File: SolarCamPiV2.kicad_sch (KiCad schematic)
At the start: 95 parts, among them J1 TagConnect_TC2030_SWD, J2 RPi, J3 FTDI_RPI, Q1 AO3401A, Q2 AO3401A, Q3 2N7002, Q4 AO3401A, Q5 2N7002, Q6 BSS84, SW1 User, U1 CN3767, U2 HT7533, U3 SY8113B, U4 STM32G031Fx, Y1 32.768kHz

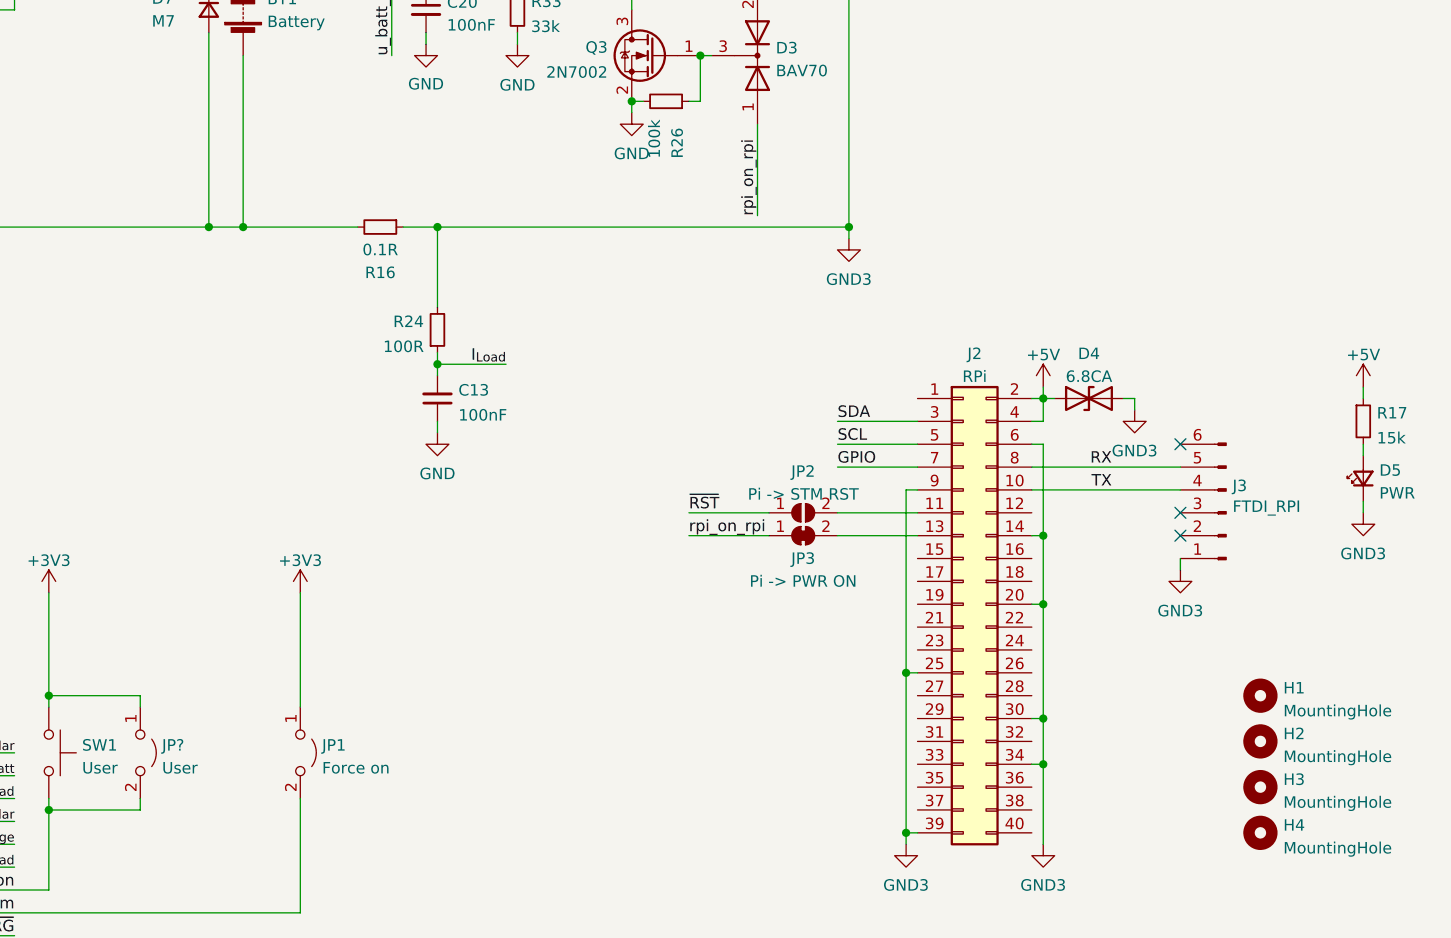
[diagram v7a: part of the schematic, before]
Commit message: Connect SWD to RPi GPIOs
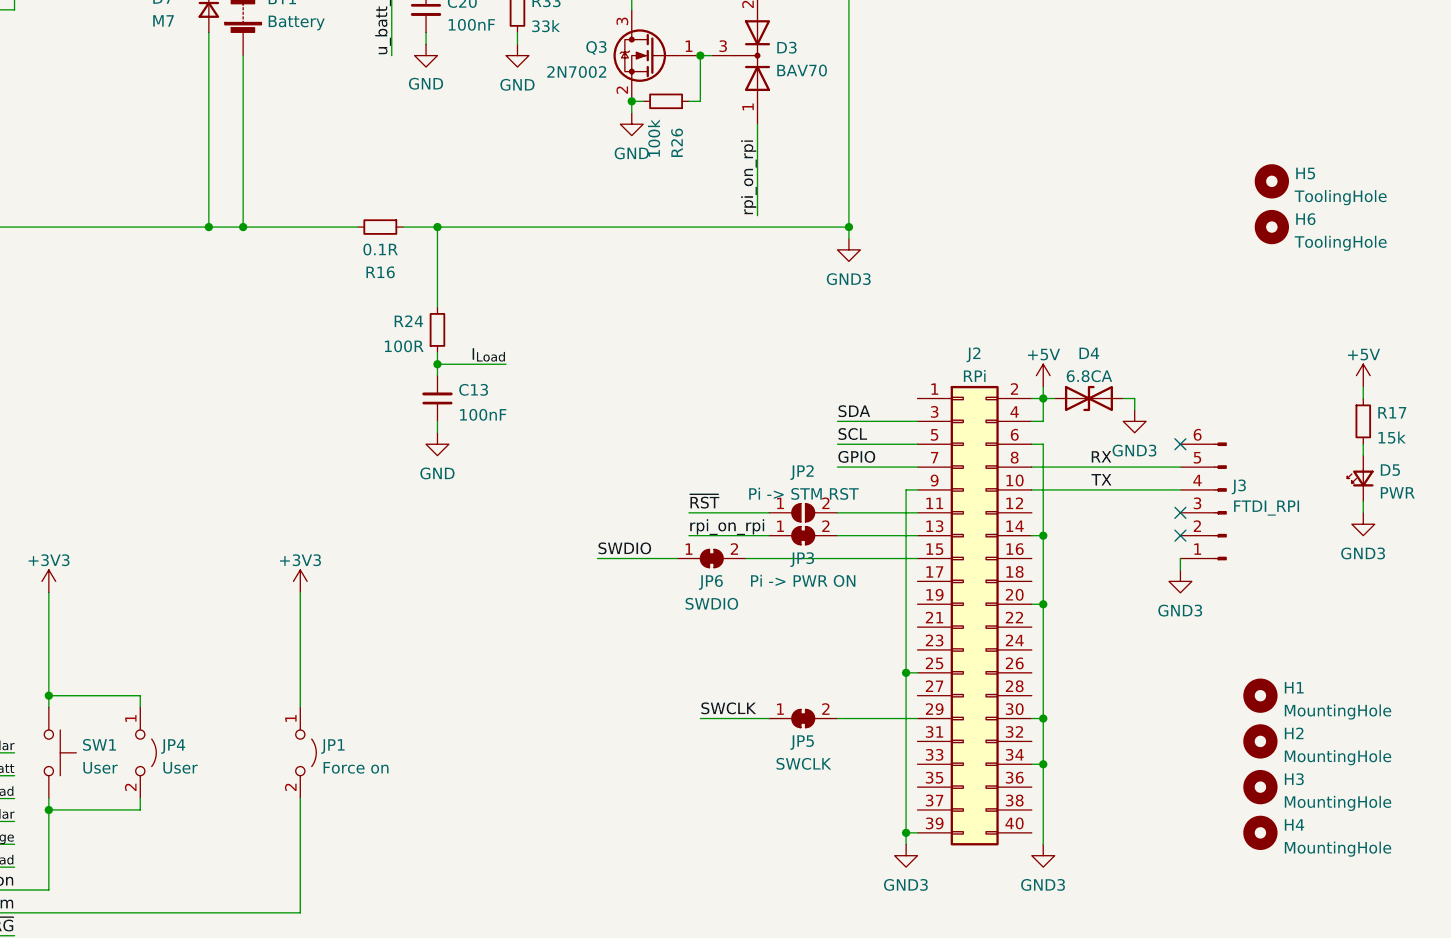
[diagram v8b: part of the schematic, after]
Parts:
- added H5, H6: ToolingHole, ToolingHole:ToolingHole_JLCSMT, symbol Mechanical:MountingHole
- added JP5: SWCLK, Jumper:SolderJumper-2_P1.3mm_Bridged_Pad1.0x1.5mm, symbol Jumper:SolderJumper_2_Bridged
- added JP6: SWDIO, Jumper:SolderJumper-2_P1.3mm_Bridged_Pad1.0x1.5mm, symbol Jumper:SolderJumper_2_Bridged
- H1, H2, H3, H4, J1: now left out of the parts list
- gave numbers to parts that had none: 1
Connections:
- net SWCLK: now also JP5.1 (A)
- net SWDIO: now also JP6.1 (A)
- net at J2.15 (Pin_15): now also JP6.2 (B)
- net at J2.29 (Pin_29): now also JP5.2 (B)
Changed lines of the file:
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@@
     (stroke (width 0) (type default) (color 0 0 0 0))
   )
+  (wire (pts (xy 218.44 144.78) (xy 227.33 144.78))
+    (stroke (width 0) (type default) (color 0 0 0 0))
+  )
   (wire (pts (xy 46.99 53.34) (xy 55.88 53.34))
     (stroke (width 0) (type default) (color 0 0 0 0))
@@
     (stroke (width 0) (type default) (color 0 0 0 0))
   )
+  (wire (pts (xy 191.77 127) (xy 200.66 127))
+    (stroke (width 0) (type default) (color 0 0 0 0))
+  )
   (wire (pts (xy 83.82 105.41) (xy 83.82 106.68))
     (stroke (width 0) (type default) (color 0 0 0 0))
@@
     (stroke (width 0) (type default) (color 0 0 0 0))
   )
+  (wire (pts (xy 208.28 127) (xy 227.33 127))
+    (stroke (width 0) (type default) (color 0 0 0 0))
+  )
   (wire (pts (xy 86.36 22.86) (xy 86.36 39.37))
     (stroke (width 0) (type default) (color 0 0 0 0))
@@
     (stroke (width 0) (type default) (color 0 0 0 0))
   )
+  (wire (pts (xy 203.2 144.78) (xy 210.82 144.78))
+    (stroke (width 0) (type default) (color 0 0 0 0))
+  )
   (wire (pts (xy 246.38 39.37) (xy 255.27 39.37))
     (stroke (width 0) (type default) (color 0 0 0 0))
@@
     (effects (font (size 1.27 1.27)) (justify left bottom))
   )
+  (label "SWCLK" (at 203.2 144.78 0)
+    (effects (font (size 1.27 1.27)) (justify left bottom))
+  )
   (label "I_{Charge}" (at 127 158.75 180)
     (effects (font (size 1.27 1.27)) (justify right bottom))
@@
     (effects (font (size 1.27 1.27)) (justify left bottom))
   )
+  (label "SWDIO" (at 191.77 127 0)
+    (effects (font (size 1.27 1.27)) (justify left bottom))
+  )
   (label "U_{Solar}" (at 127 148.59 180)
     (effects (font (size 1.27 1.27)) (justify right bottom))
@@
     (pin "2")
   )
+  (symbol (lib_id "Jumper:SolderJumper_2_Bridged") (at 204.47 127 0) (unit 1)
+    (in_bom yes) (on_board yes)
+    (property "Reference" "JP6" (id 0) (at 204.47 129.5431 0))
+    (property "Value" "SWDIO" (id 1) (at 204.47 132.08 0))
+    (property "Footprint" "Jumper:SolderJumper-2_P1.3mm_Bridged_Pad1.0x1.5mm" (id 2) (at 204.47 127 0)
+      (effects (font (size 1.27 1.27)) hide)
+    )
+    (property "Datasheet" "~" (id 3) (at 204.47 127 0)
+      (effects (font (size 1.27 1.27)) hide)
+    )
+    (pin "1")
+    (pin "2")
+  )
   (symbol (lib_id "power:+3V3") (at 52.07 140.97 0) (unit 1)
     (in_bom yes) (on_board yes) (fields_autoplaced)
@@
     (pin "2")
   )
+  (symbol (lib_id "Mechanical:MountingHole") (at 266.7 90.17 0) (unit 1)
+    (in_bom no) (on_board yes) (fields_autoplaced)
+    (property "Reference" "H6" (id 0) (at 269.24 89.3353 0)
+      (effects (font (size 1.27 1.27)) (justify left))
+    )
+    (property "Value" "ToolingHole" (id 1) (at 269.24 91.8722 0)
+      (effects (font (size 1.27 1.27)) (justify left))
+    )
+    (property "Footprint" "ToolingHole:ToolingHole_JLCSMT" (id 2) (at 266.7 90.17 0)
+      (effects (font (size 1.27 1.27)) hide)
+    )
+    (property "Datasheet" "~" (id 3) (at 266.7 90.17 0)
+      (effects (font (size 1.27 1.27)) hide)
+    )
+  )
   (symbol (lib_id "Device:C_Small") (at 37.8384 135.5727 180) (unit 1)
     (in_bom yes) (on_board yes) (fields_autoplaced)
@@
   )
   (symbol (lib_id "Mechanical:MountingHole") (at 265.43 147.32 0) (unit 1)
-    (in_bom yes) (on_board yes) (fields_autoplaced)
+    (in_bom no) (on_board yes) (fields_autoplaced)
     (property "Reference" "H2" (id 0) (at 267.97 146.4853 0)
       (effects (font (size 1.27 1.27)) (justify left))
@@
   )
   (symbol (lib_id "Connector_TagConnect:TagConnect_TC2030_SWD") (at 149.86 179.07 0) (mirror y) (unit 1)
-    (in_bom yes) (on_board yes) (fields_autoplaced)
+    (in_bom no) (on_board yes) (fields_autoplaced)
     (property "Reference" "J1" (id 0) (at 149.86 171.5602 0))
     (property "Value" "TagConnect_TC2030_SWD" (id 1) (at 149.86 174.0971 0))
@@
   (symbol (lib_id "Jumper:Jumper_2_Open") (at 140.97 148.59 270) (unit 1)
     (in_bom yes) (on_board yes) (fields_autoplaced)
-    (property "Reference" "JP?" (id 0) (at 143.383 147.7553 90)
+    (property "Reference" "JP4" (id 0) (at 143.383 147.7553 90)
       (effects (font (size 1.27 1.27)) (justify left))
     )
@@
   )
   (symbol (lib_id "Mechanical:MountingHole") (at 265.43 157.48 0) (unit 1)
-    (in_bom yes) (on_board yes) (fields_autoplaced)
+    (in_bom no) (on_board yes) (fields_autoplaced)
     (property "Reference" "H4" (id 0) (at 267.97 156.6453 0)
       (effects (font (size 1.27 1.27)) (justify left))
@@
   )
   (symbol (lib_id "Mechanical:MountingHole") (at 265.43 152.4 0) (unit 1)
-    (in_bom yes) (on_board yes) (fields_autoplaced)
+    (in_bom no) (on_board yes) (fields_autoplaced)
     (property "Reference" "H3" (id 0) (at 267.97 151.5653 0)
       (effects (font (size 1.27 1.27)) (justify left))
@@
     (pin "6")
   )
+  (symbol (lib_id "Jumper:SolderJumper_2_Bridged") (at 214.63 144.78 0) (unit 1)
+    (in_bom yes) (on_board yes)
+    (property "Reference" "JP5" (id 0) (at 214.63 147.3231 0))
+    (property "Value" "SWCLK" (id 1) (at 214.63 149.86 0))
+    (property "Footprint" "Jumper:SolderJumper-2_P1.3mm_Bridged_Pad1.0x1.5mm" (id 2) (at 214.63 144.78 0)
+      (effects (font (size 1.27 1.27)) hide)
+    )
+    (property "Datasheet" "~" (id 3) (at 214.63 144.78 0)
+      (effects (font (size 1.27 1.27)) hide)
+    )
+    (pin "1")
+    (pin "2")
+  )
   (symbol (lib_id "Device:C_Small") (at 83.82 109.22 180) (unit 1)
     (in_bom yes) (on_board yes) (fields_autoplaced)
@@
   )
   (symbol (lib_id "Mechanical:MountingHole") (at 265.43 142.24 0) (unit 1)
-    (in_bom yes) (on_board yes) (fields_autoplaced)
+    (in_bom no) (on_board yes) (fields_autoplaced)
     (property "Reference" "H1" (id 0) (at 267.97 141.4053 0)
       (effects (font (size 1.27 1.27)) (justify left))
@@
     (pin "1")
   )
+  (symbol (lib_id "Mechanical:MountingHole") (at 266.7 85.09 0) (unit 1)
+    (in_bom no) (on_board yes) (fields_autoplaced)
+    (property "Reference" "H5" (id 0) (at 269.24 84.2553 0)
+      (effects (font (size 1.27 1.27)) (justify left))
+    )
+    (property "Value" "ToolingHole" (id 1) (at 269.24 86.7922 0)
+      (effects (font (size 1.27 1.27)) (justify left))
+    )
+    (property "Footprint" "ToolingHole:ToolingHole_JLCSMT" (id 2) (at 266.7 85.09 0)
+      (effects (font (size 1.27 1.27)) hide)
+    )
+    (property "Datasheet" "~" (id 3) (at 266.7 85.09 0)
+      (effects (font (size 1.27 1.27)) hide)
+    )
+  )
   (symbol (lib_id "Device:R_Small") (at 262.89 50.8 180) (unit 1)
     (in_bom yes) (on_board yes)
@@
       (reference "H4") (unit 1) (value "MountingHole") (footprint "MountingHole:MountingHole_2.7mm_M2.5")
     )
+    (path "/f8c7e76d-e31d-4321-acab-771ee3545261"
+      (reference "H5") (unit 1) (value "ToolingHole") (footprint "ToolingHole:ToolingHole_JLCSMT")
+    )
+    (path "/335fc768-9fd3-455e-8f5d-f2d937b01570"
+      (reference "H6") (unit 1) (value "ToolingHole") (footprint "ToolingHole:ToolingHole_JLCSMT")
+    )
     (path "/62cf0445-6004-4cb2-9971-00ef4b908d3f"
       (reference "J1") (unit 1) (value "TagConnect_TC2030_SWD") (footprint "Connector:Tag-Connect_TC2030-IDC-NL_2x03_P1.27mm_Vertical")
@@
     )
     (path "/80c79d4c-bd1e-491d-9024-cf67191a104a"
-      (reference "JP?") (unit 1) (value "User") (footprint "Connector_PinHeader_2.54mm:PinHeader_1x02_P2.54mm_Horizontal")
+      (reference "JP4") (unit 1) (value "User") (footprint "Connector_PinHeader_2.54mm:PinHeader_1x02_P2.54mm_Horizontal")
+    )
+    (path "/b8c47ae7-e306-4fdc-ae6d-24ab80cd55cd"
+      (reference "JP5") (unit 1) (value "SWCLK") (footprint "Jumper:SolderJumper-2_P1.3mm_Bridged_Pad1.0x1.5mm")
+    )
+    (path "/22cd4a75-1362-45c7-94c4-88f7ed05dae7"
+      (reference "JP6") (unit 1) (value "SWDIO") (footprint "Jumper:SolderJumper-2_P1.3mm_Bridged_Pad1.0x1.5mm")
     )
     (path "/41956ed0-8edb-4799-b456-d49581251475"
